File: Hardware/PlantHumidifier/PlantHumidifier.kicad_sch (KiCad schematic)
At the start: 10 parts, among them J1 Conn_01x04_Female, J2 Conn_01x05_Female, J3 Conn_01x04_Female, J4 Conn_01x04_Female, SW1 SW_SPST, U1 WeMos_D1_mini

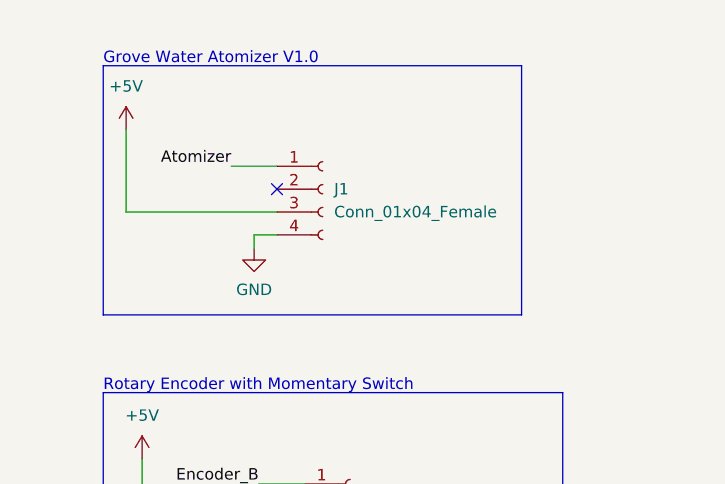
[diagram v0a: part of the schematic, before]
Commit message: Schematic: Add symbol/Footprints for atomizer and finish footprint assignment
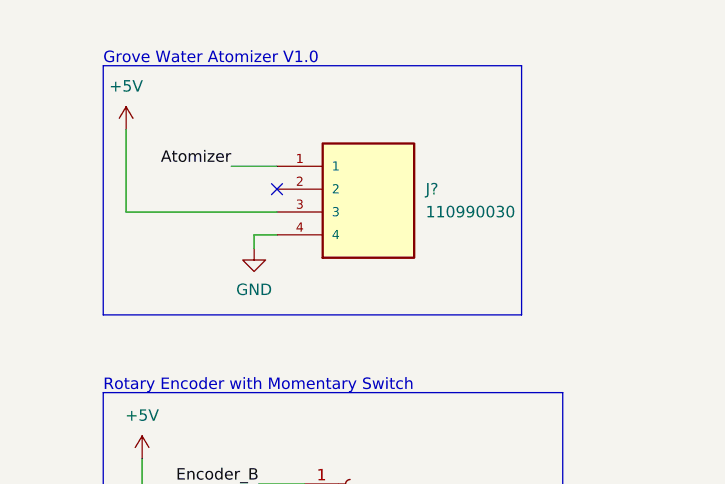
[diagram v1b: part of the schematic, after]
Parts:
- removed J1: Conn_01x04_Female, Connector_JST:JST_PH_B4B-PH-K_1x04_P2.00mm_Vertical, symbol Connector:Conn_01x04_Female
- added J?: 110990030, Seeed_Connectors:SEEED_110990030, symbol 110990030:110990030
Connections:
- net +5V: now also J?.3
- net Atomizer: now also J?.1
- net GND: now also J?.4
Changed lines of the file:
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@@
     (pin "2")
-  )
-  (symbol (lib_id "Connector:Conn_01x04_Female") (at 200.66 32.766 0) (unit 1)
-    (in_bom yes) (on_board yes) (fields_autoplaced)
-    (property "Reference" "J1" (id 0) (at 201.93 32.7659 0)
-      (effects (font (size 1.27 1.27)) (justify left))
-    )
-    (property "Value" "Conn_01x04_Female" (id 1) (at 201.93 35.3059 0)
-      (effects (font (size 1.27 1.27)) (justify left))
-    )
-    (property "Footprint" "Connector_JST:JST_PH_B4B-PH-K_1x04_P2.00mm_Vertical" (id 2) (at 200.66 32.766 0)
-      (effects (font (size 1.27 1.27)) hide)
-    )
-    (property "Datasheet" "~" (id 3) (at 200.66 32.766 0)
-      (effects (font (size 1.27 1.27)) hide)
-    )
-    (pin "1")
-    (pin "2")
-    (pin "3")
-    (pin "4")
   )
   (symbol (lib_id "power:GND") (at 59.69 65.024 180) (unit 1)
@@
     )
     (pin "1")
+  )
+  (symbol (lib_id "110990030:110990030") (at 205.74 32.766 0) (unit 1)
+    (in_bom yes) (on_board yes) (fields_autoplaced)
+    (property "Reference" "J?" (id 0) (at 212.09 32.7659 0)
+      (effects (font (size 1.27 1.27)) (justify left))
+    )
+    (property "Value" "110990030" (id 1) (at 212.09 35.3059 0)
+      (effects (font (size 1.27 1.27)) (justify left))
+    )
+    (property "Footprint" "Seeed_Connectors:SEEED_110990030" (id 2) (at 205.74 32.766 0)
+      (effects (font (size 1.27 1.27)) (justify bottom) hide)
+    )
+    (property "Datasheet" "" (id 3) (at 205.74 32.766 0)
+      (effects (font (size 1.27 1.27)) hide)
+    )
+    (property "MAXIMUM_PACKAGE_HEIGHT" "8.1mm" (id 4) (at 205.74 32.766 0)
+      (effects (font (size 1.27 1.27)) (justify bottom) hide)
+    )
+    (property "PARTREV" "A" (id 5) (at 205.74 32.766 0)
+      (effects (font (size 1.27 1.27)) (justify bottom) hide)
+    )
+    (property "MANUFACTURER" "Seeed Technology" (id 6) (at 205.74 32.766 0)
+      (effects (font (size 1.27 1.27)) (justify bottom) hide)
+    )
+    (property "STANDARD" "Manufacturer Recommendations" (id 7) (at 205.74 32.766 0)
+      (effects (font (size 1.27 1.27)) (justify bottom) hide)
+    )
+    (pin "1")
+    (pin "2")
+    (pin "3")
+    (pin "4")
   )
   (symbol (lib_id "MCU_Module:WeMos_D1_mini") (at 115.316 108.458 0) (unit 1)
@@
       (reference "C2") (unit 1) (value "100n") (footprint "Capacitor_SMD:C_0402_1005Metric")
     )
-    (path "/2394e559-b98a-40f6-b850-791be34e4734"
-      (reference "J1") (unit 1) (value "Conn_01x04_Female") (footprint "Connector_JST:JST_PH_B4B-PH-K_1x04_P2.00mm_Vertical")
-    )
     (path "/b462574f-43c5-4a1a-9527-fc39d017b1e6"
       (reference "J2") (unit 1) (value "Conn_01x05_Female") (footprint "Connector_JST:JST_XH_B5B-XH-A_1x05_P2.50mm_Vertical")
@@
       (reference "J4") (unit 1) (value "Conn_01x04_Female") (footprint "Connector_JST:JST_XH_B4B-XH-A_1x04_P2.50mm_Vertical")
     )
+    (path "/f617cd1b-909f-4cbb-bc4d-a14076c52ab4"
+      (reference "J?") (unit 1) (value "110990030") (footprint "Seeed_Connectors:SEEED_110990030")
+    )
     (path "/e7e820f3-59b8-44fe-b769-6d65c3132a62"

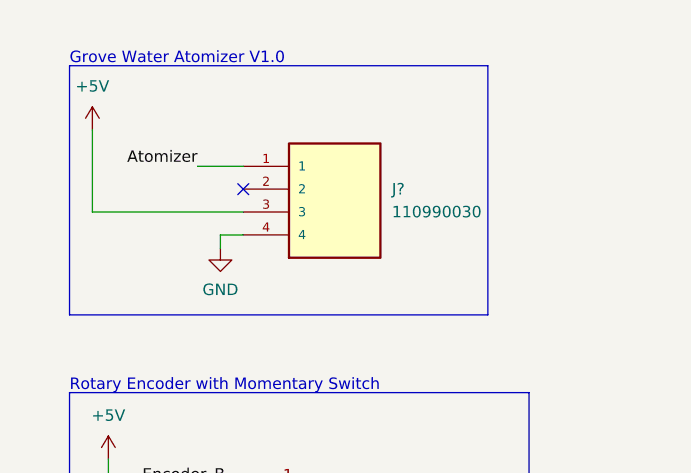
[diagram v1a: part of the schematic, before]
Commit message: Schematic: Fix unlabeled part and run ERC again
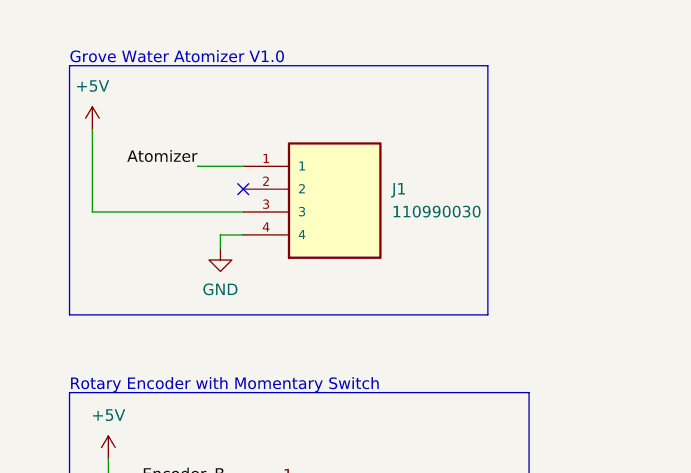
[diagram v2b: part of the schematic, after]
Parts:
- gave numbers to parts that had none: 1
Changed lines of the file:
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@@
   (symbol (lib_id "110990030:110990030") (at 205.74 32.766 0) (unit 1)
     (in_bom yes) (on_board yes) (fields_autoplaced)
-    (property "Reference" "J?" (id 0) (at 212.09 32.7659 0)
+    (property "Reference" "J1" (id 0) (at 212.09 32.7659 0)
       (effects (font (size 1.27 1.27)) (justify left))
     )
@@
       (reference "C2") (unit 1) (value "100n") (footprint "Capacitor_SMD:C_0402_1005Metric")
     )
+    (path "/f617cd1b-909f-4cbb-bc4d-a14076c52ab4"
+      (reference "J1") (unit 1) (value "110990030") (footprint "Seeed_Connectors:SEEED_110990030")
+    )
     (path "/b462574f-43c5-4a1a-9527-fc39d017b1e6"
       (reference "J2") (unit 1) (value "Conn_01x05_Female") (footprint "Connector_JST:JST_XH_B5B-XH-A_1x05_P2.50mm_Vertical")
@@
       (reference "J4") (unit 1) (value "Conn_01x04_Female") (footprint "Connector_JST:JST_XH_B4B-XH-A_1x04_P2.50mm_Vertical")
     )
-    (path "/f617cd1b-909f-4cbb-bc4d-a14076c52ab4"
-      (reference "J?") (unit 1) (value "110990030") (footprint "Seeed_Connectors:SEEED_110990030")
-    )
     (path "/e7e820f3-59b8-44fe-b769-6d65c3132a62"

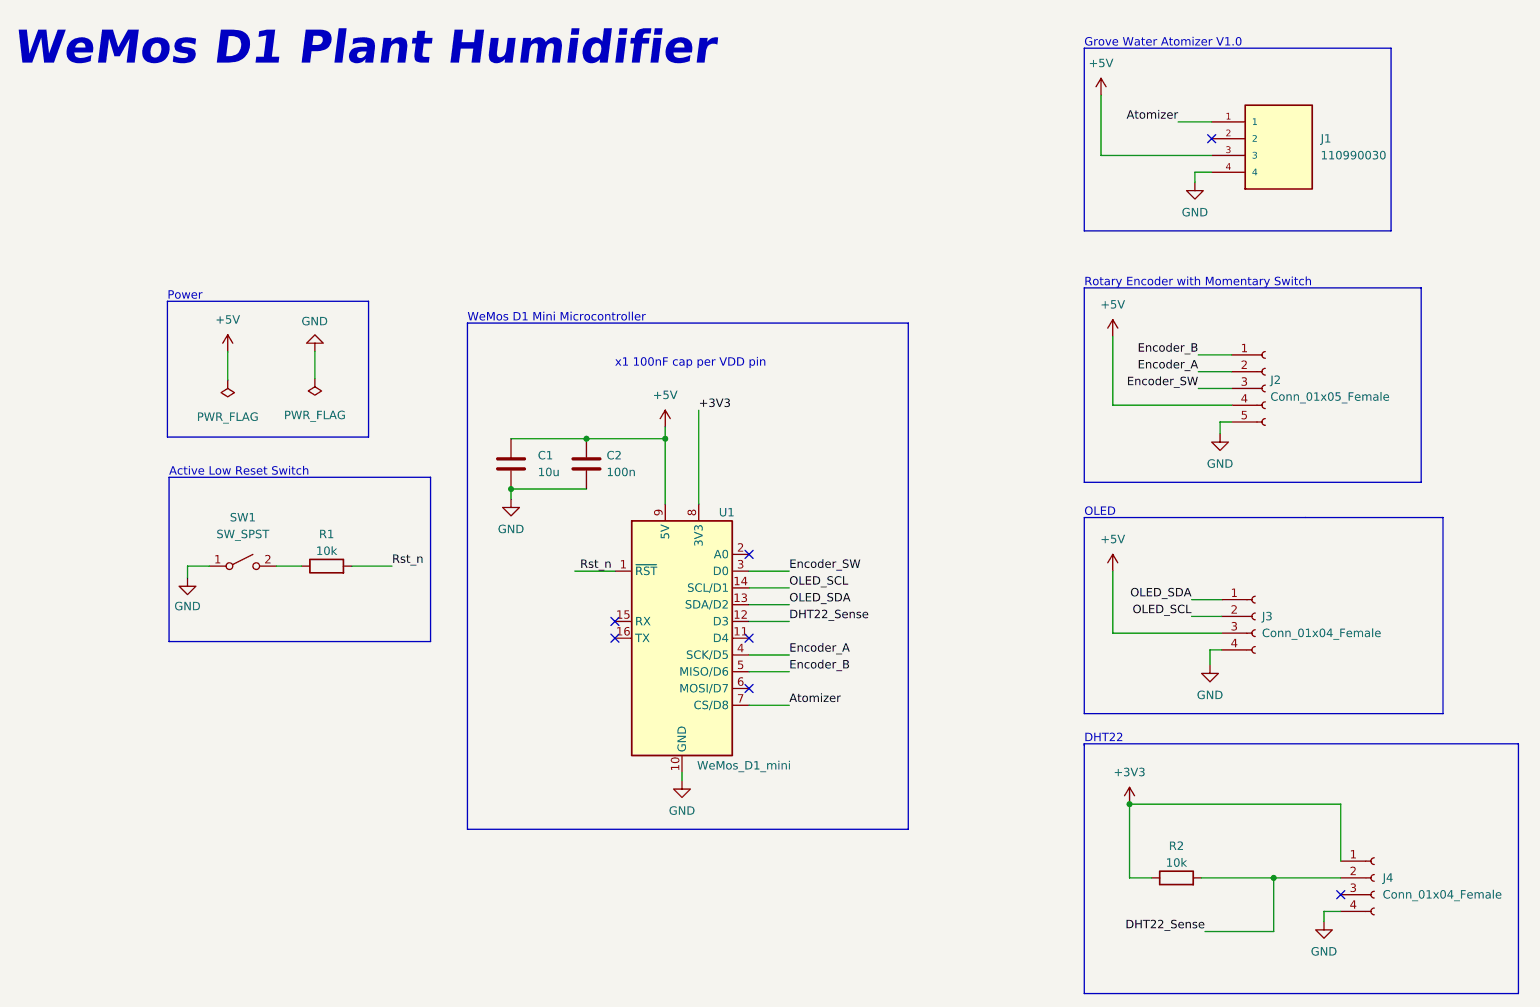
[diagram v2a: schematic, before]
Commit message: Schematic: Reflect changes in pin assignment
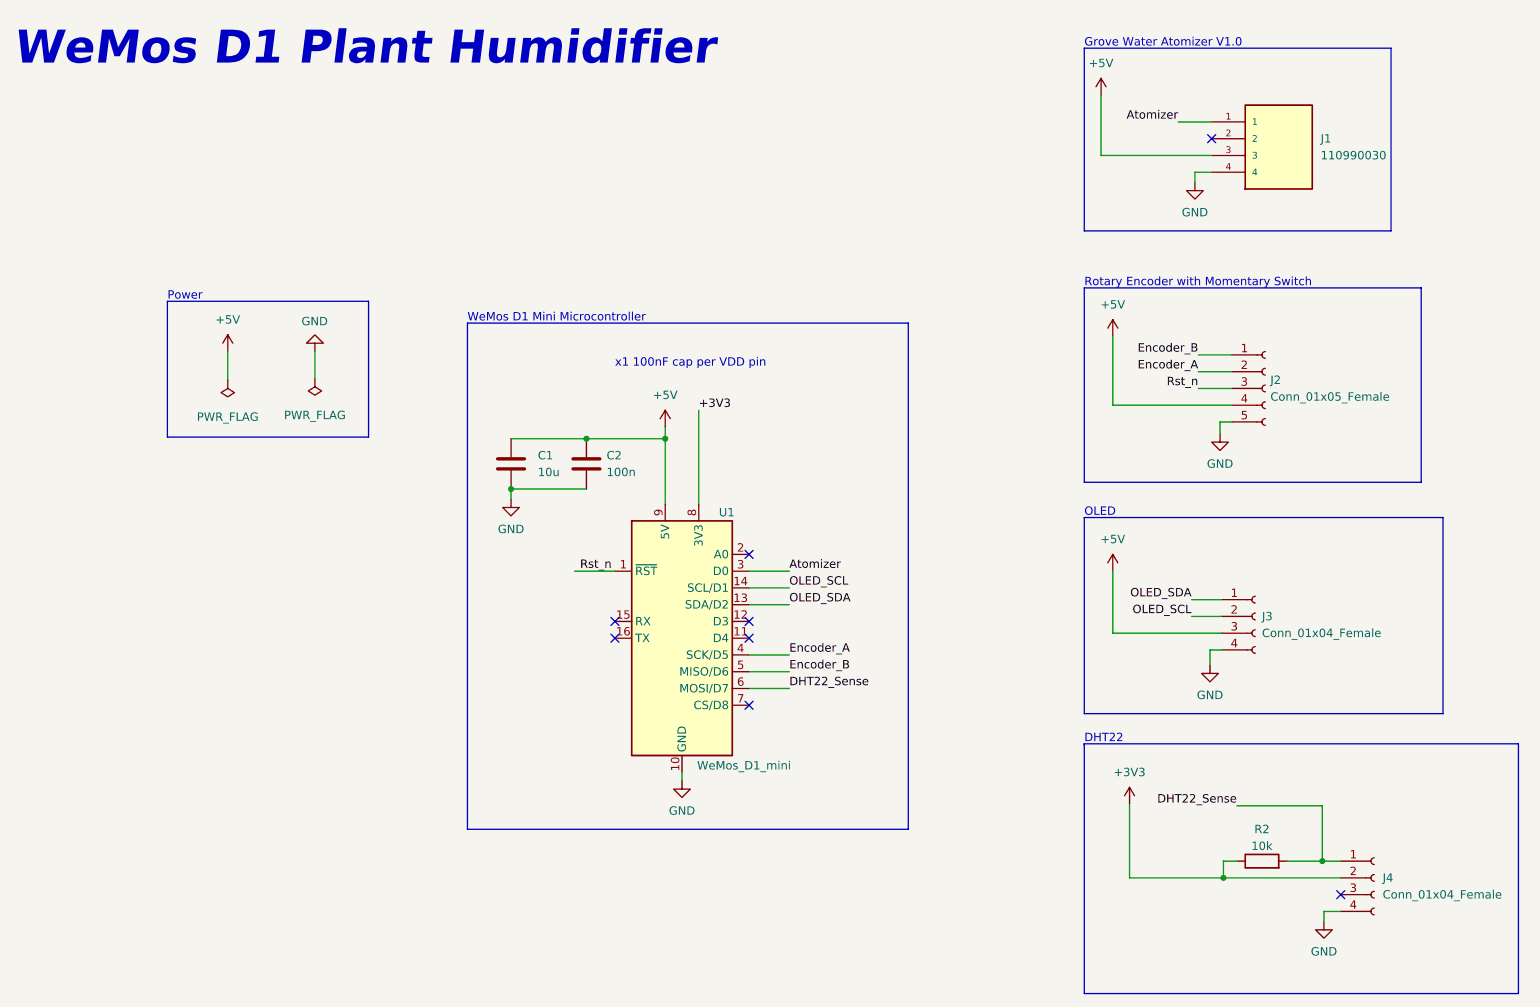
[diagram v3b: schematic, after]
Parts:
- removed R1: 10k, Resistor_SMD:R_0402_1005Metric, symbol Device:R
- removed SW1: SW_SPST, Button_Switch_THT:SW_Tactile_SPST_Angled_PTS645Vx83-2LFS, symbol Switch:SW_SPST
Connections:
- net +3V3: now also J4.2 (Pin_2); no longer J4.1 (Pin_1)
- net Atomizer: now also U1.3 (D0); no longer U1.7 (CS/D8)
- net DHT22_Sense: now also J4.1 (Pin_1), U1.6 (MOSI/D7); no longer J4.2 (Pin_2), U1.12 (D3)
- net Rst_n: now also J2.3 (Pin_3)
- removed net Encoder_SW: J2.3 (Pin_3), U1.3 (D0)
- no-connect marks 7 -> 8
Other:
- note removed: "Active Low Reset Switch"
- moved on the sheet: R2

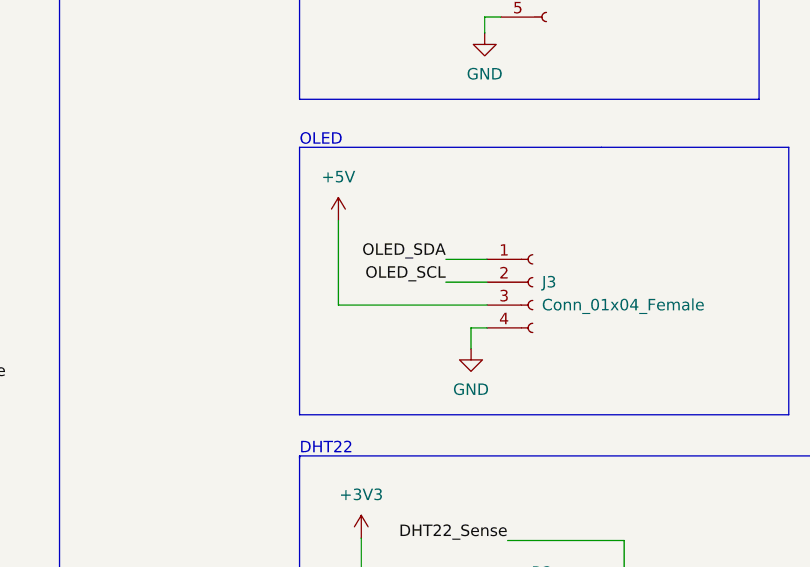
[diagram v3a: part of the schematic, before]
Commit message: Change pin assignment for OLED for better routing
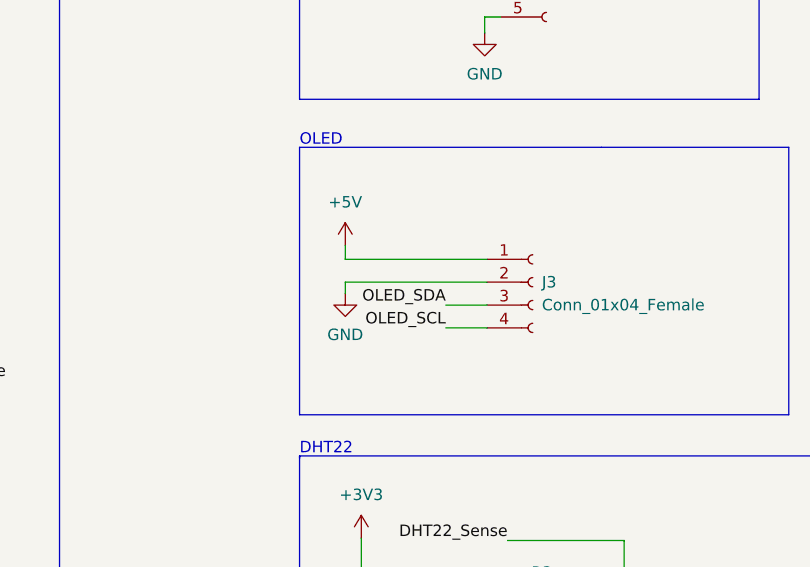
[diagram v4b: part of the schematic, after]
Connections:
- net +5V: now also J3.1 (Pin_1); no longer J3.3 (Pin_3)
- net GND: now also J3.2 (Pin_2); no longer J3.4 (Pin_4)
- net OLED_SCL: now also J3.4 (Pin_4); no longer J3.2 (Pin_2)
- net OLED_SDA: now also J3.3 (Pin_3); no longer J3.1 (Pin_1)
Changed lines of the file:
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@@
     (stroke (width 0) (type default) (color 0 0 0 0))
   )
-  (wire (pts (xy 192.532 105.156) (xy 197.104 105.156))
+  (wire (pts (xy 192.532 110.236) (xy 197.104 110.236))
     (stroke (width 0) (type default) (color 0 0 0 0))
   )
@@
     (stroke (width 0) (type default) (color 0 0 0 0))
   )
-  (wire (pts (xy 192.532 102.616) (xy 197.104 102.616))
+  (wire (pts (xy 192.532 107.696) (xy 197.104 107.696))
     (stroke (width 0) (type default) (color 0 0 0 0))
   )
@@
     (stroke (width 0) (type default) (color 0 0 0 0))
   )
+  (wire (pts (xy 181.356 102.616) (xy 197.104 102.616))
+    (stroke (width 0) (type default) (color 0 0 0 0))
+  )
   (polyline (pts (xy 176.276 19.05) (xy 176.276 46.736))
     (stroke (width 0) (type default) (color 0 0 0 0))
@@
     (stroke (width 0) (type default) (color 0 0 0 0))
   )
-  (wire (pts (xy 197.104 107.696) (xy 180.594 107.696))
-    (stroke (width 0) (type default) (color 0 0 0 0))
-  )
   (polyline (pts (xy 176.276 90.17) (xy 176.276 119.888))
     (stroke (width 0) (type default) (color 0 0 0 0))
@@
     (stroke (width 0) (type default) (color 0 0 0 0))
   )
-  (wire (pts (xy 180.594 98.298) (xy 180.594 107.696))
+  (wire (pts (xy 181.356 101.092) (xy 181.356 102.616))
     (stroke (width 0) (type default) (color 0 0 0 0))
   )
@@
     (stroke (width 0) (type default) (color 0 0 0 0))
   )
-  (wire (pts (xy 195.326 110.236) (xy 197.104 110.236))
+  (wire (pts (xy 181.356 105.156) (xy 197.104 105.156))
     (stroke (width 0) (type default) (color 0 0 0 0))
   )
@@
     (stroke (width 0) (type default) (color 0 0 0 0))
   )
-  (wire (pts (xy 195.326 112.522) (xy 195.326 110.236))
-    (stroke (width 0) (type default) (color 0 0 0 0))
-  )
   (wire (pts (xy 212.598 149.86) (xy 212.598 151.384))
     (stroke (width 0) (type default) (color 0 0 0 0))
@@
   )
   (polyline (pts (xy 82.804 60.706) (xy 149.606 60.706))
+    (stroke (width 0) (type default) (color 0 0 0 0))
+  )
+  (wire (pts (xy 181.356 105.156) (xy 181.356 106.426))
     (stroke (width 0) (type default) (color 0 0 0 0))
   )
@@
     (effects (font (size 1.27 1.27)) (justify left bottom))
   )
-  (label "OLED_SCL" (at 192.532 105.156 180)
+  (label "OLED_SCL" (at 192.532 110.236 180)
     (effects (font (size 1.27 1.27)) (justify right bottom))
   )
@@
     (effects (font (size 1.27 1.27)) (justify left bottom))
   )
-  (label "OLED_SDA" (at 192.532 102.616 180)
+  (label "OLED_SDA" (at 192.532 107.696 180)
     (effects (font (size 1.27 1.27)) (justify right bottom))
   )
@@
     (pin "1")
   )
-  (symbol (lib_id "power:+5V") (at 180.594 98.298 0) (unit 1)
-    (in_bom yes) (on_board yes) (fields_autoplaced)
-    (property "Reference" "#PWR09" (id 0) (at 180.594 102.108 0)
-      (effects (font (size 1.27 1.27)) hide)
-    )
-    (property "Value" "+5V" (id 1) (at 180.594 93.472 0))
-    (property "Footprint" "" (id 2) (at 180.594 98.298 0)
-      (effects (font (size 1.27 1.27)) hide)
-    )
-    (property "Datasheet" "" (id 3) (at 180.594 98.298 0)
+  (symbol (lib_id "power:+5V") (at 181.356 101.092 0) (unit 1)
+    (in_bom yes) (on_board yes) (fields_autoplaced)
+    (property "Reference" "#PWR09" (id 0) (at 181.356 104.902 0)
+      (effects (font (size 1.27 1.27)) hide)
+    )
+    (property "Value" "+5V" (id 1) (at 181.356 96.266 0))
+    (property "Footprint" "" (id 2) (at 181.356 101.092 0)
+      (effects (font (size 1.27 1.27)) hide)
+    )
+    (property "Datasheet" "" (id 3) (at 181.356 101.092 0)
       (effects (font (size 1.27 1.27)) hide)
     )
@@
     (pin "2")
   )
-  (symbol (lib_id "power:GND") (at 195.326 112.522 0) (unit 1)
-    (in_bom yes) (on_board yes) (fields_autoplaced)
-    (property "Reference" "#PWR011" (id 0) (at 195.326 118.872 0)
-      (effects (font (size 1.27 1.27)) hide)
-    )
-    (property "Value" "GND" (id 1) (at 195.326 117.094 0))
-    (property "Footprint" "" (id 2) (at 195.326 112.522 0)
-      (effects (font (size 1.27 1.27)) hide)
-    )
-    (property "Datasheet" "" (id 3) (at 195.326 112.522 0)
-      (effects (font (size 1.27 1.27)) hide)
-    )
+  (symbol (lib_id "power:GND") (at 181.356 106.426 0) (unit 1)
+    (in_bom yes) (on_board yes) (fields_autoplaced)
+    (property "Reference" "#PWR011" (id 0) (at 181.356 112.776 0)
+      (effects (font (size 1.27 1.27)) hide)
+    )
+    (property "Value" "GND" (id 1) (at 181.356 110.998 0))
+    (property "Footprint" "" (id 2) (at 181.356 106.426 0)
+      (effects (font (size 1.27 1.27)) hide)
+    )
+    (property "Datasheet" "" (id 3) (at 181.356 106.426 0)
+      (effects (font (size 1.27 1.27)) hide)
+    )
